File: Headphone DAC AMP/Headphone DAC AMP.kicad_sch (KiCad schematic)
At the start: 1 part, among them J3 SJ-3502-SMT

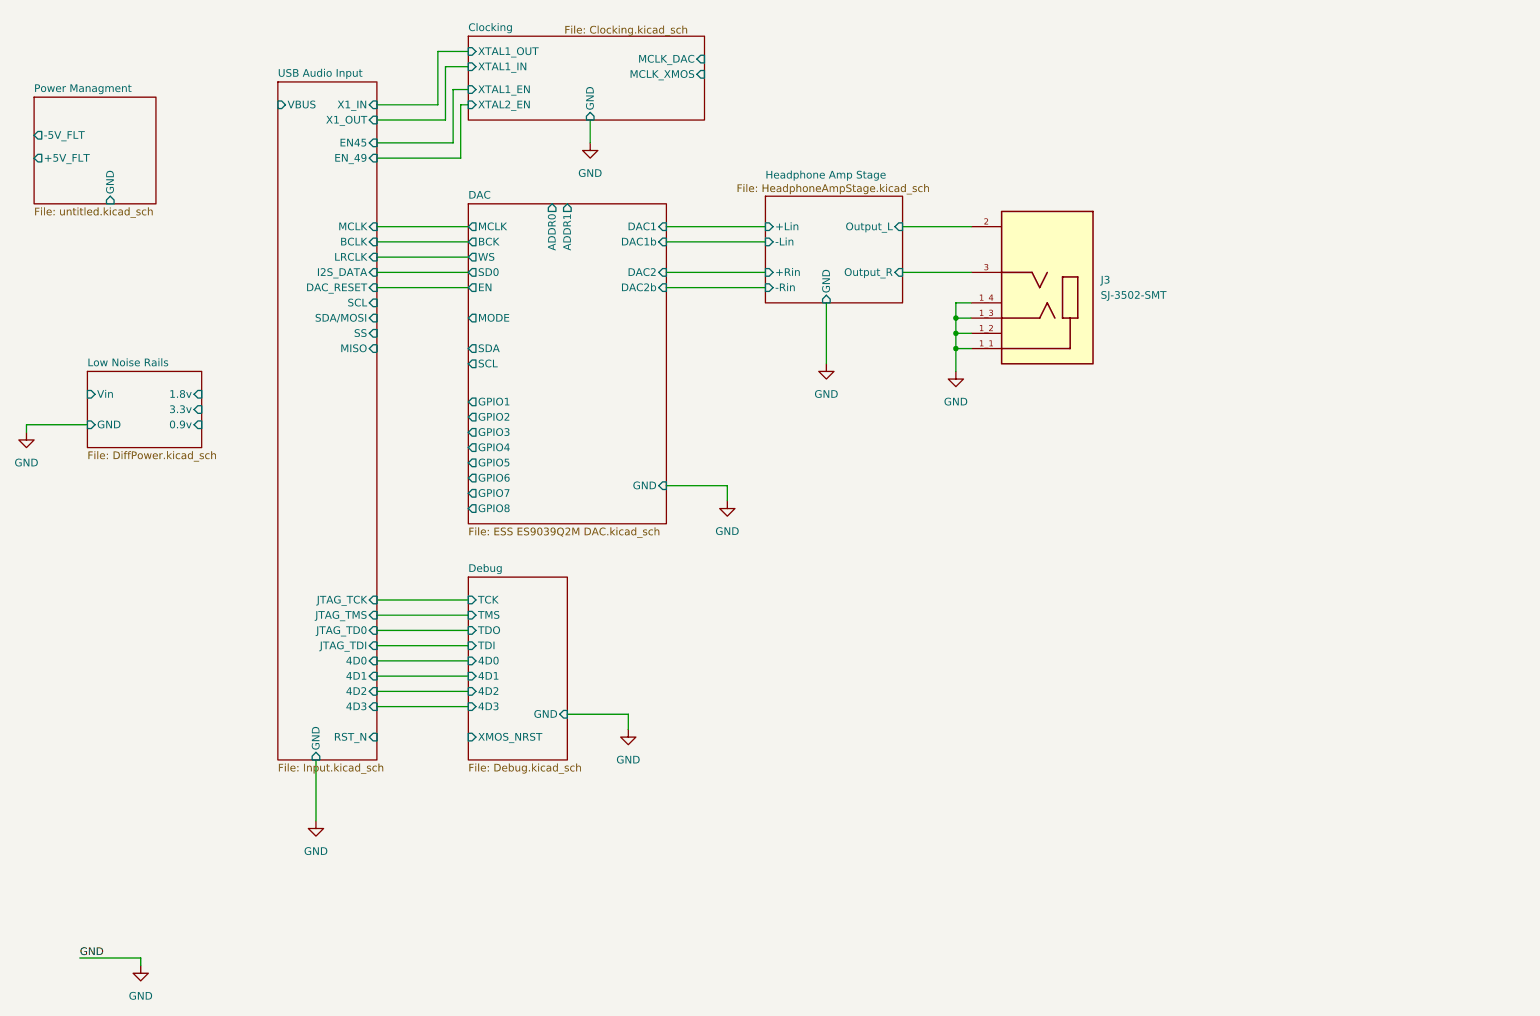
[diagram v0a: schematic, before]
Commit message: Polished DAC GPIOs and connected to XMOS
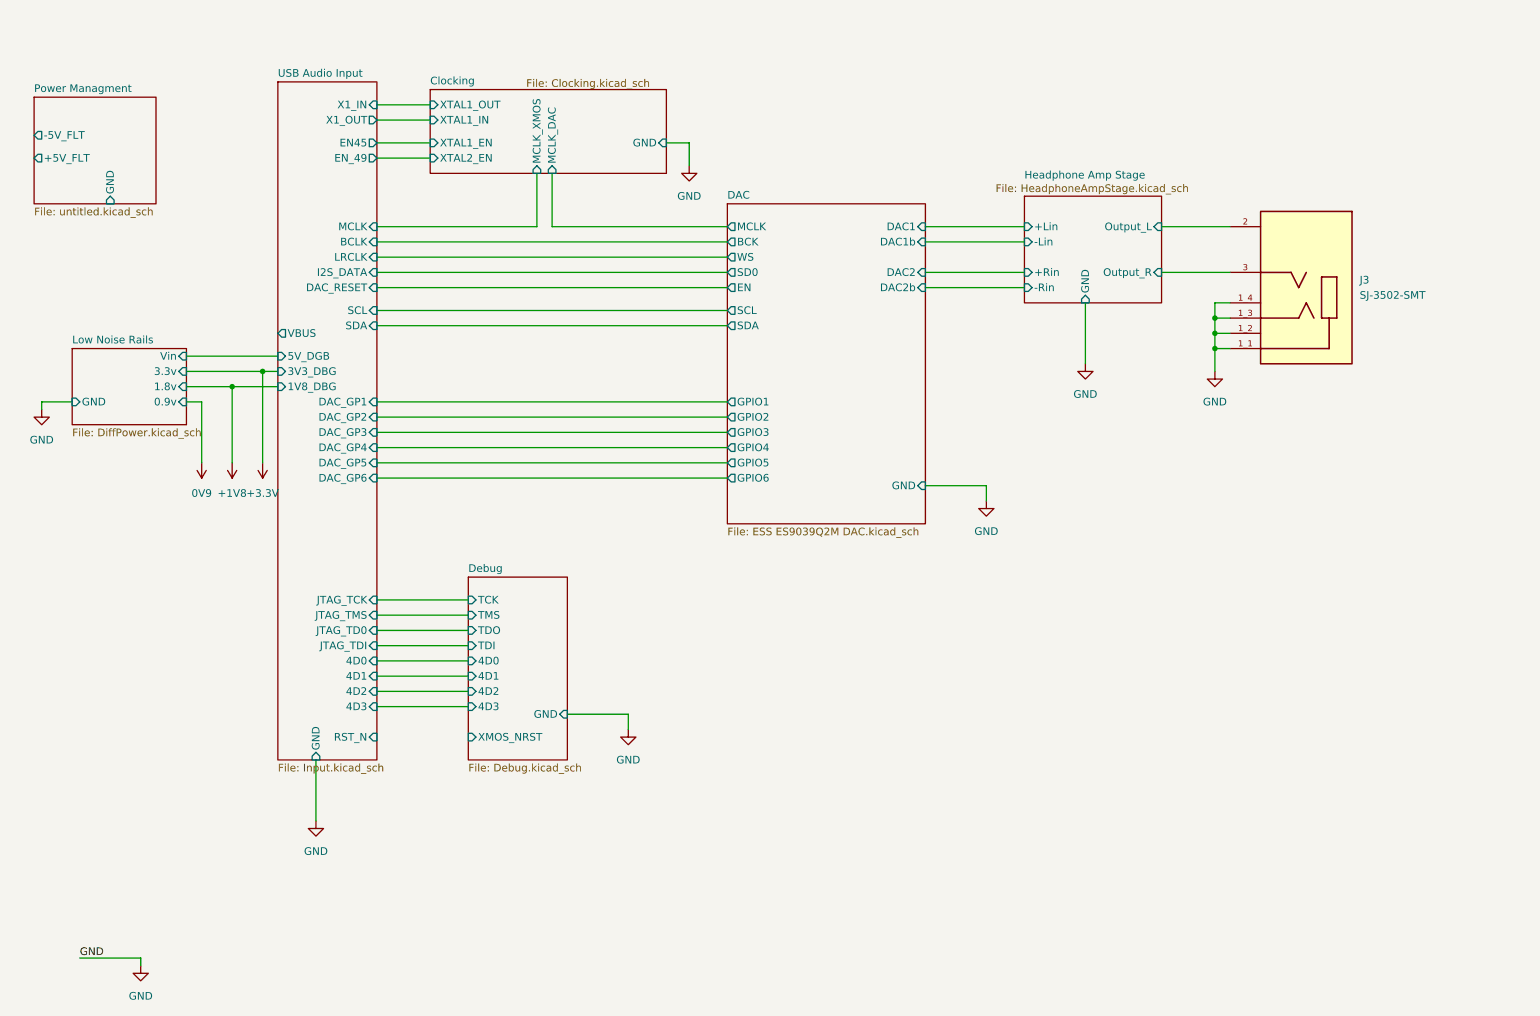
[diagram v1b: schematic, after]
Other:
- sheet DAC ports: added none; removed ADDR0, ADDR1, GPIO7, GPIO8, MODE
- sheet USB Audio Input ports: added 1V8_DBG, 3V3_DBG, 5V_DGB, DAC_GP1, DAC_GP2, DAC_GP3, DAC_GP4, DAC_GP5, DAC_GP6, SDA; removed MISO, SDA/MOSI, SS
- moved on the sheet: J3

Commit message: Cleaned Up and Annotated Schematic
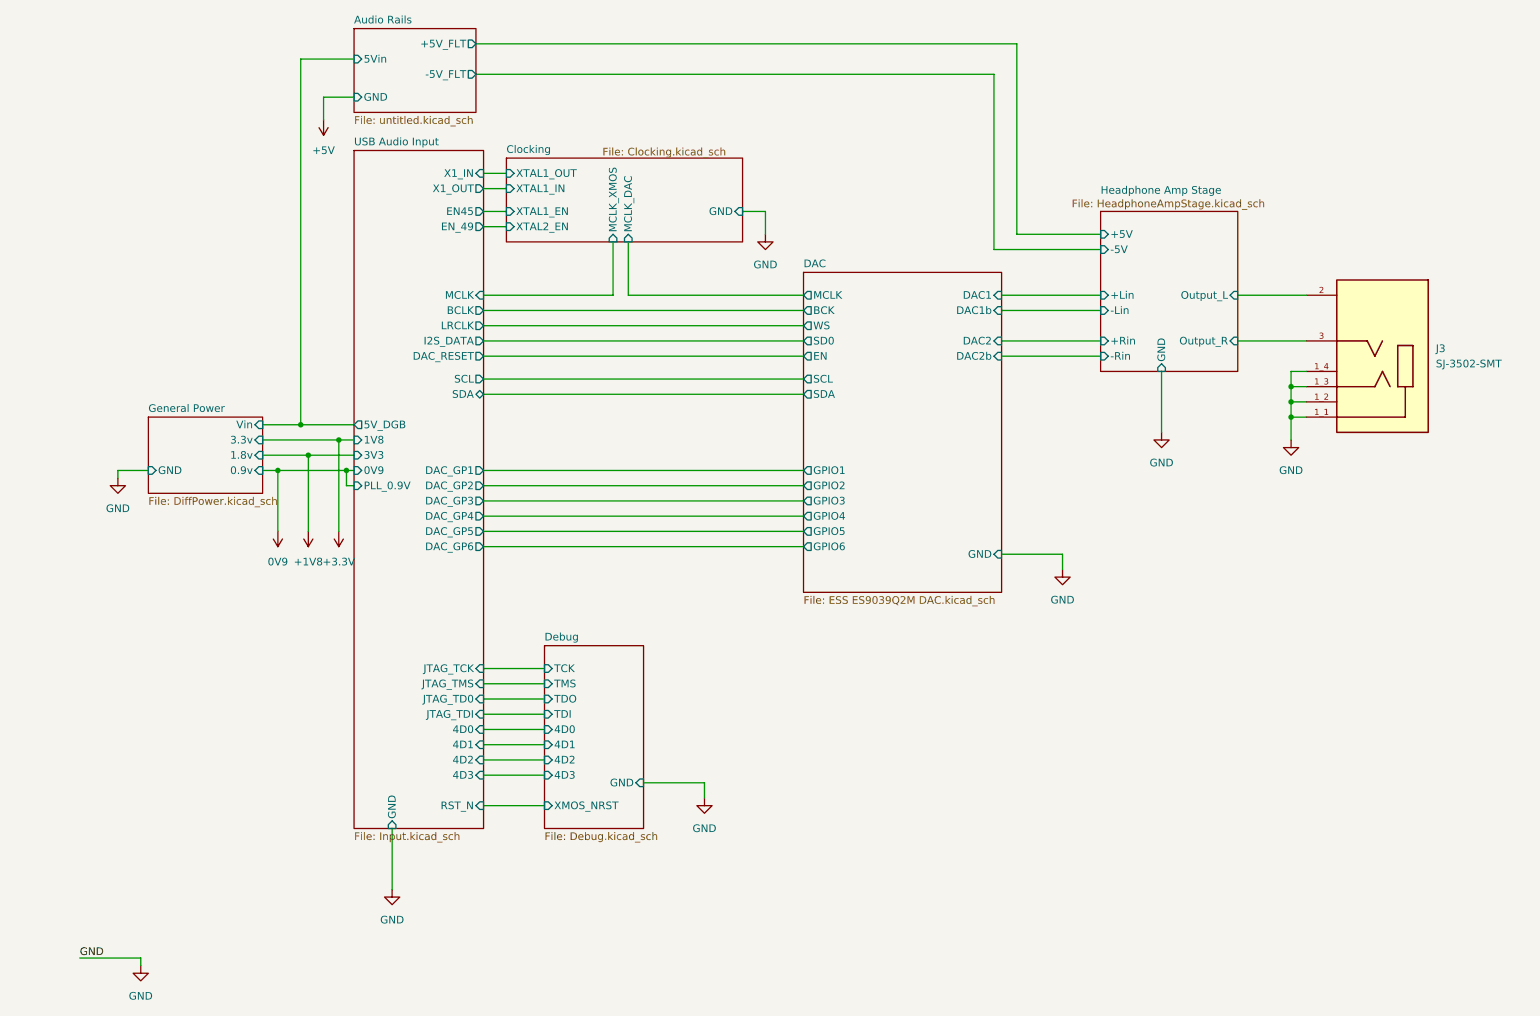
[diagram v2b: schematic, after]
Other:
- sheet Low Noise Rails renamed General Power
- sheet Power Managment renamed Audio Rails
- sheet Audio Rails ports: added 5Vin; removed none
- sheet Headphone Amp Stage ports: added +5V, -5V; removed none
- sheet USB Audio Input ports: added 0V9, 1V8, 3V3, PLL_0.9V; removed 1V8_DBG, 3V3_DBG, VBUS
- company: (none) -> Personal Project - Kettering University
- title: (none) -> Hi-Fidelity USB DAC Amplifier
- moved on the sheet: J3

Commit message: Schematic V1 Done
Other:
- note added: "DEBUGGING"
- note added: "GPIO"
- note added: "I2C"
- note added: "I2S"
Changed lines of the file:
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@@
 		(comment 2 "Based on XMOS Xu316 and ES9039Q2M")
+	)
+	(text "I2C"
+		(exclude_from_sim no)
+		(at 115.824 86.614 0)
+		(effects
+			(font
+				(size 4 4)
+				(thickness 0.8)
+				(bold yes)
+				(color 0 194 0 1)
+			)
+		)
+	)
+	(text "DEBUGGING"
+		(exclude_from_sim no)
+		(at 95.25 145.288 90)
+		(effects
+			(font
+				(size 3 3)
+				(thickness 0.8)
+				(bold yes)
+				(color 0 194 0 1)
+			)
+		)
+	)
+	(text "I2S"
+		(exclude_from_sim no)
+		(at 112.268 76.454 0)
+		(effects
+			(font
+				(size 5 5)
+				(thickness 1)
+				(bold yes)
+				(color 0 194 0 1)
+			)
+		)
+	)
+	(text "GPIO"
+		(exclude_from_sim no)
+		(at 115.57 106.68 0)
+		(effects
+			(font
+				(size 5 5)
+				(thickness 1)
+				(bold yes)
+				(color 0 194 0 1)
+			)
+		)
 	)
 	(junction
@@
 	(symbol
 		(lib_id "power:+1V8")
-		(at 63.5 41.91 180)
-		(unit 1)
-		(exclude_from_sim no)
-		(in_bom yes)
-		(on_board yes)
-		(dnp no)
-		(fields_autoplaced yes)
-		(property "Reference" "#PWR0112"
-			(at 63.5 38.1 0)
-			(effects
-				(font
-					(size 1.27 1.27)
-				)
-				(hide yes)
-			)
-		)
-		(property "Value" "+5V"
-			(at 63.5 46.99 0)
-			(effects
-				(font
-					(size 1.27 1.27)
-				)
-			)
-		)
-		(property "Footprint" ""
-			(at 63.5 41.91 0)
-			(effects
-				(font
-					(size 1.27 1.27)
-				)
-				(hide yes)
-			)
-		)
-		(property "Datasheet" ""
-			(at 63.5 41.91 0)
-			(effects
-				(font
-					(size 1.27 1.27)
-				)
-				(hide yes)
-			)
-		)
-		(property "Description" "Power symbol creates a global label with name \"+1V8\""
-			(at 63.5 41.91 0)
-			(effects
-				(font
-					(size 1.27 1.27)
-				)
-				(hide yes)
-			)
-		)
-		(pin "1"
-		)
-		(instances
-			(project "Headphone DAC AMP"
-				(path "/d034eddd-efbc-47be-a25c-37cbfbab4cd8"
-					(reference "#PWR0112")
-					(unit 1)
-				)
-			)
-		)
-	)
-	(symbol
-		(lib_id "power:+1V8")
 		(at 55.88 110.49 180)
 		(unit 1)
@@
 					(unit 1)
 				)
+			)
+		)
+	)
+	(symbol
+		(lib_id "power:GND")
+		(at 63.5 41.91 0)
+		(unit 1)
+		(exclude_from_sim no)
+		(in_bom yes)
+		(on_board yes)
+		(dnp no)
+		(fields_autoplaced yes)
+		(property "Reference" "#PWR0112"
+			(at 63.5 48.26 0)
+			(effects
+				(font
+					(size 1.27 1.27)
+				)
+				(hide yes)
+			)
+		)
+		(property "Value" "GND"
+			(at 63.5 46.99 0)
+			(effects
+				(font
+					(size 1.27 1.27)
+				)
+			)
+		)
+		(property "Footprint" ""
+			(at 63.5 41.91 0)
+			(effects
+				(font
+					(size 1.27 1.27)
+				)
+				(hide yes)
+			)
+		)
+		(property "Datasheet" ""
+			(at 63.5 41.91 0)
+			(effects
+				(font
+					(size 1.27 1.27)
+				)
+				(hide yes)
+			)
+		)
+		(property "Description" "Power symbol creates a global label with name \"GND\" , ground"
+			(at 63.5 41.91 0)
+			(effects
+				(font
+					(size 1.27 1.27)
+				)
+				(hide yes)
+			)
+		)
+		(pin "1"
+		)
+		(instances
+			(project "Headphone DAC AMP"
+				(path "/d034eddd-efbc-47be-a25c-37cbfbab4cd8"
+					(reference "#PWR0112")
+					(unit 1)
+				)

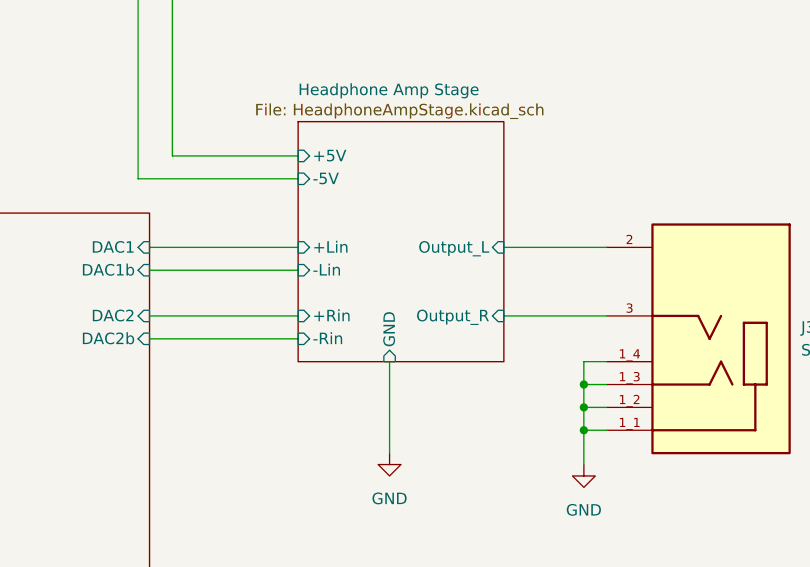
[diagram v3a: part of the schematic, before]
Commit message: Footprints & Placements
All footprints are loaded in PCB error free, some PCB mistakes were fixed, and worked on the placements for the TPA6120, the XMOS, the DAC, and the outputs
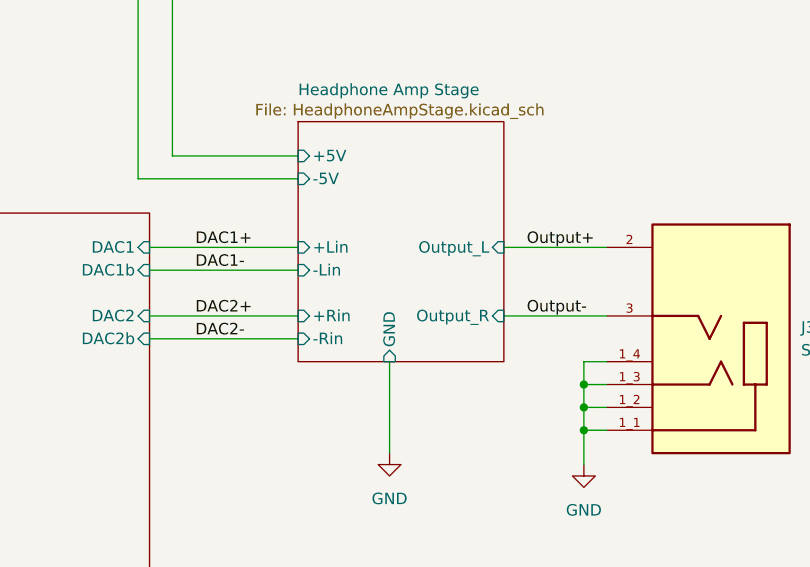
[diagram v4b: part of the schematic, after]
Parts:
- J3: footprint SJ-3502-SMT:CUI_SJ-3502-SMT -> SJ_3502_SMT_TR:CUI_SJ-3502-SMT
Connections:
- net Headphone Amp Stage/Output_L renamed Output+
- net Headphone Amp Stage/Output_R renamed Output-
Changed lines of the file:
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@@
+		)
+	)
+	(label "DAC2+"
+		(at 181.61 78.74 0)
+		(effects
+			(font
+				(size 1.27 1.27)
+			)
+			(justify left bottom)
+		)
+	)
+	(label "Output-"
+		(at 218.44 78.74 0)
+		(effects
+			(font
+				(size 1.27 1.27)
+			)
+			(justify left bottom)
+		)
+	)
+	(label "DAC1-"
+		(at 181.61 73.66 0)
+		(effects
+			(font
+				(size 1.27 1.27)
+			)
+			(justify left bottom)
+		)
+	)
+	(label "Output+"
+		(at 218.44 71.12 0)
+		(effects
+			(font
+				(size 1.27 1.27)
+			)
+			(justify left bottom)
+		)
+	)
+	(label "DAC1+"
+		(at 181.61 71.12 0)
+		(effects
+			(font
+				(size 1.27 1.27)
+			)
+			(justify left bottom)
+		)
+	)
+	(label "DAC2-"
+		(at 181.61 81.28 0)
+		(effects
+			(font
+				(size 1.27 1.27)
+			)
+			(justify left bottom)
 		)
 	)
@@
 			)
 		)
-		(property "Footprint" "SJ-3502-SMT:CUI_SJ-3502-SMT"
+		(property "Footprint" "SJ_3502_SMT_TR:CUI_SJ-3502-SMT"
 			(at 240.03 86.36 0)
 			(effects

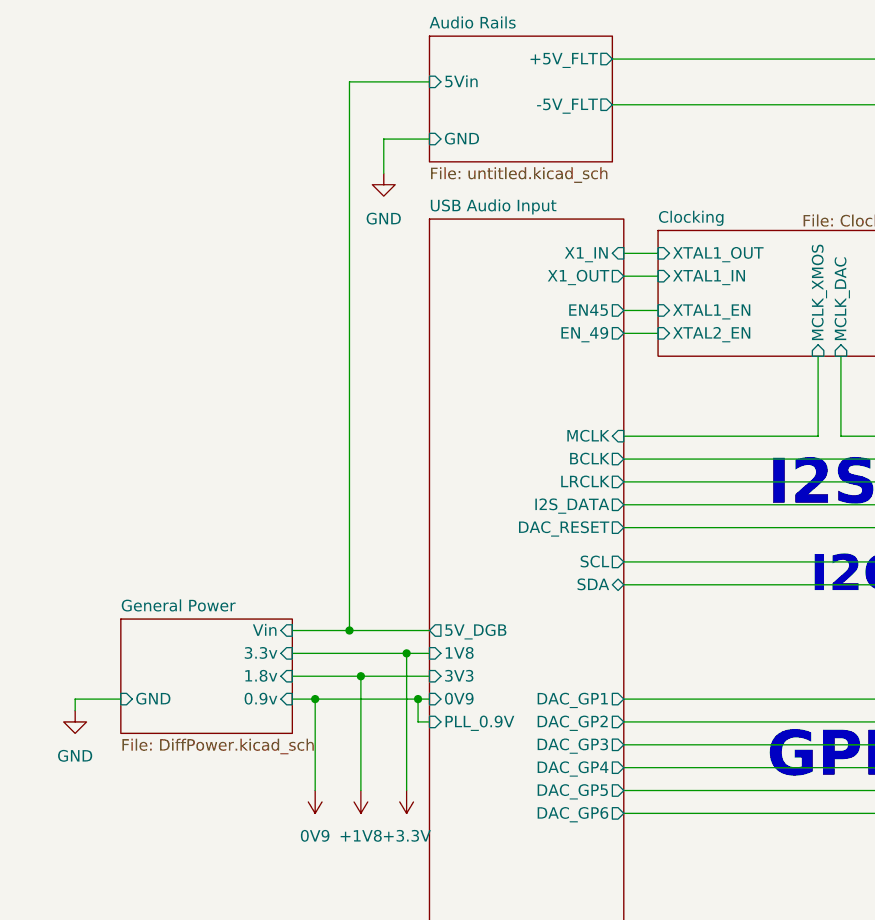
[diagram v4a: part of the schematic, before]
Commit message: Cleaned up schematic for posting a review
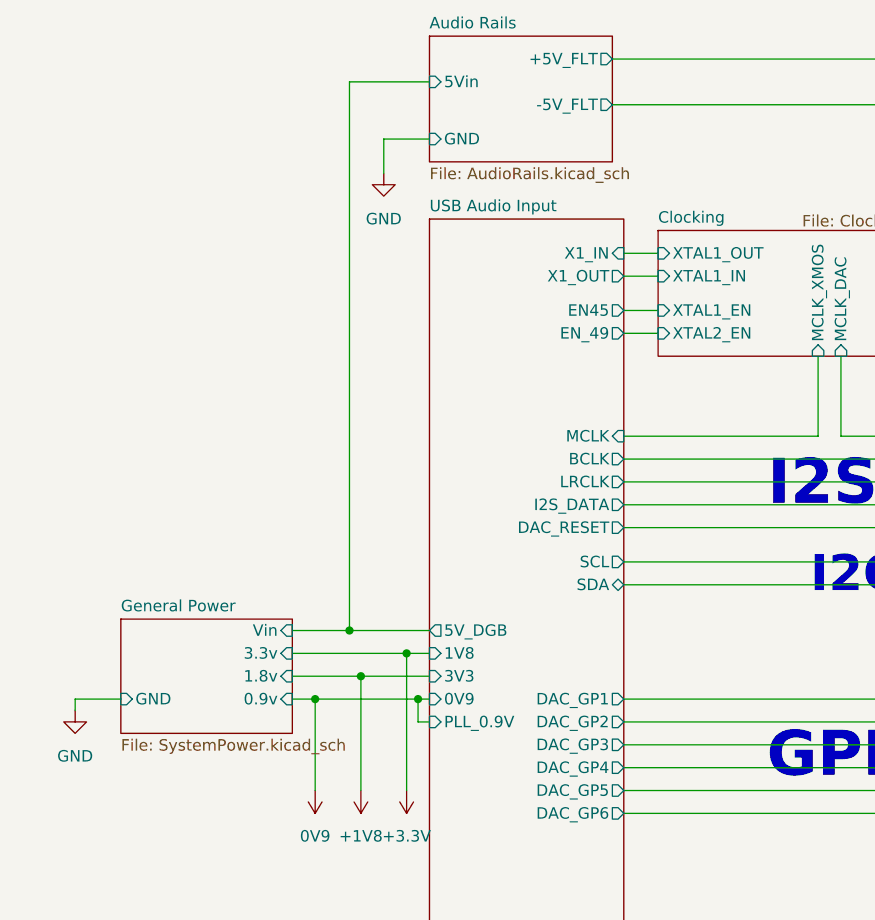
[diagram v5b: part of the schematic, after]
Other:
- sheet Audio Rails: file untitled.kicad_sch -> AudioRails.kicad_sch
- sheet General Power: file DiffPower.kicad_sch -> SystemPower.kicad_sch
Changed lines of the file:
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@@
 		)
 		(fill
-			(color 0 0 0 0.0000)
+			(color 0 0 194 0.5000)
 		)
 		(property "Sheetname" "Debug"
@@
 		)
 		(fill
-			(color 0 0 0 0.0000)
+			(color 132 0 0 1.0000)
 		)
 		(property "Sheetname" "Audio Rails"
@@
 			)
 		)
-		(property "Sheetfile" "untitled.kicad_sch"
+		(property "Sheetfile" "AudioRails.kicad_sch"
 			(at 68.58 41.2246 0)
 			(effects
@@
 		)
 		(fill
-			(color 0 0 0 0.0000)
+			(color 0 0 194 0.5400)
 		)
 		(property "Sheetname" "USB Audio Input"
@@
 		)
 		(fill
-			(color 0 0 0 0.0000)
+			(color 255 0 0 0.5300)
 		)
 		(property "Sheetname" "General Power"
@@
 			)
 		)
-		(property "Sheetfile" "DiffPower.kicad_sch"
+		(property "Sheetfile" "SystemPower.kicad_sch"
 			(at 34.29 104.7246 0)
 			(effects
@@
 		)
 		(fill
-			(color 0 0 0 0.0000)
+			(color 104 6 132 0.8000)
 		)
 		(property "Sheetname" "Headphone Amp Stage"
@@
 		)
 		(fill
-			(color 0 0 0 0.0000)
+			(color 104 6 132 0.8000)
 		)
 		(property "Sheetname" "DAC"
@@
 		)
 		(fill
-			(color 0 0 0 0.0000)
+			(color 0 0 194 0.5000)
 		)
 		(property "Sheetname" "Clocking"
